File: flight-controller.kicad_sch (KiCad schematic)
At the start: 15 parts, among them J1 Conn_02x10_Odd_Even, J2 Conn_02x08_Odd_Even, J3 Conn_02x17_Odd_Even, J4 Conn_02x15_Counter_Clockwise, J5 Conn_01x02, U3 ACS773LCB-100B-PFF-T

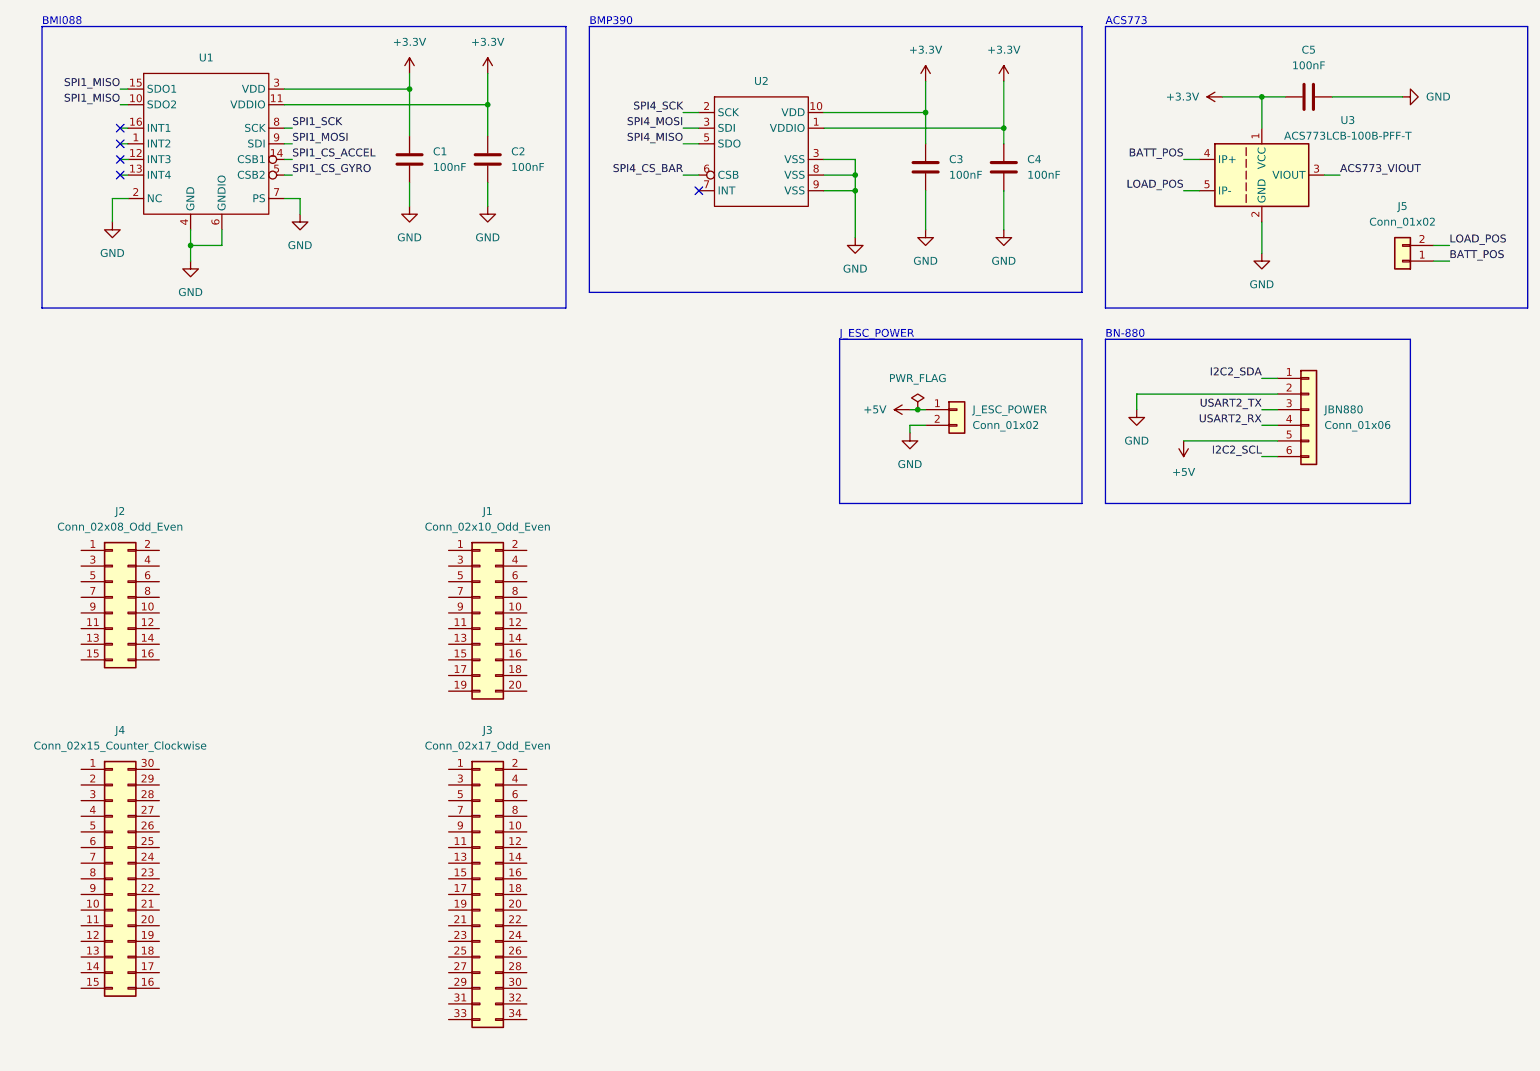
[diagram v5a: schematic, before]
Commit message: feat: Added headers of stm32 to schematic
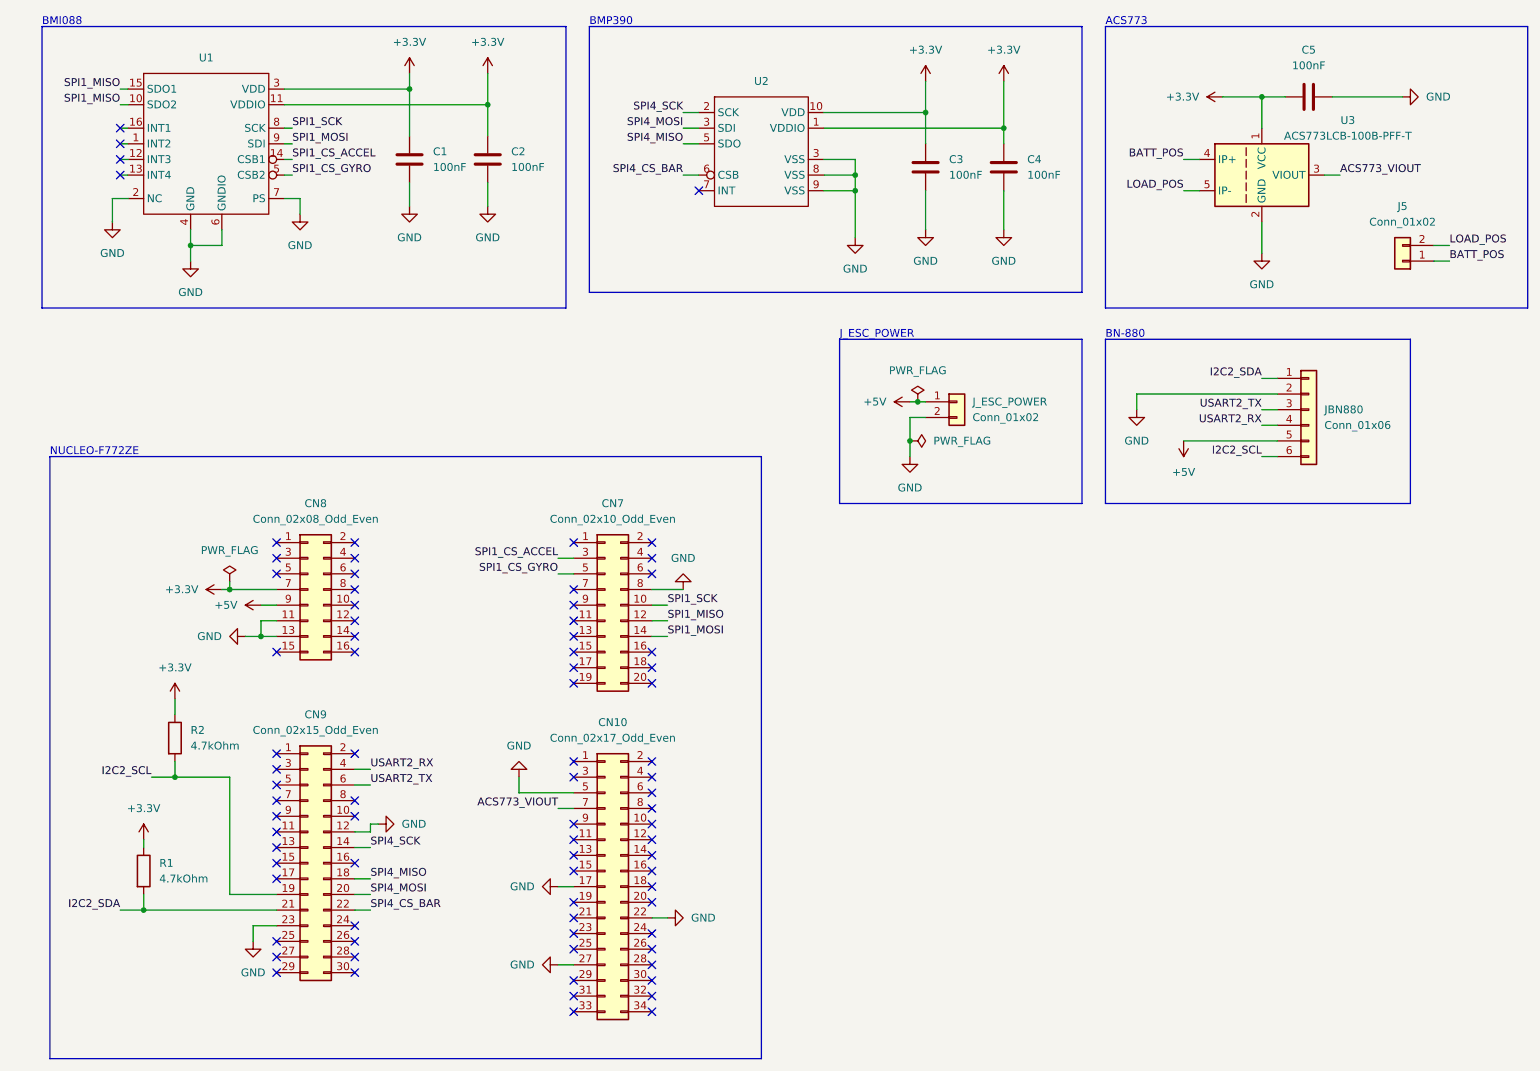
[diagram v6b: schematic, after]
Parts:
- removed J4: Conn_02x15_Counter_Clockwise, symbol Connector_Generic:Conn_02x15_Counter_Clockwise
- added CN9: Conn_02x15_Odd_Even, symbol Connector_Generic:Conn_02x15_Odd_Even
- added R1, R2: 4.7kOhm, symbol Device:R
- renumbered J3 to CN10, J1 to CN7, J2 to CN8
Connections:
- net +3.3V: now also CN8.7 (Pin_7), R1.1, R2.1
- net +5V: now also CN8.9 (Pin_9)
- net ACS773_VIOUT: now also CN10.7 (Pin_7)
- net GND: now also CN10.17 (Pin_17), CN10.22 (Pin_22), CN10.27 (Pin_27), CN10.5 (Pin_5), CN7.8 (Pin_8), CN8.11 (Pin_11), CN8.13 (Pin_13), CN9.12 (Pin_12), CN9.23 (Pin_23)
- net I2C2_SCL: now also CN9.19 (Pin_19), R2.2
- net I2C2_SDA: now also CN9.21 (Pin_21), R1.2
- net SPI1_CS_ACCEL: now also CN7.3 (Pin_3)
- net SPI1_CS_GYRO: now also CN7.5 (Pin_5)
- net SPI1_MISO: now also CN7.12 (Pin_12)
- net SPI1_MOSI: now also CN7.14 (Pin_14)
- net SPI1_SCK: now also CN7.10 (Pin_10)
- net SPI4_CS_BAR: now also CN9.22 (Pin_22)
- net SPI4_MISO: now also CN9.18 (Pin_18)
- net SPI4_MOSI: now also CN9.20 (Pin_20)
- net SPI4_SCK: now also CN9.14 (Pin_14)
- net USART2_RX: now also CN9.4 (Pin_4)
- net USART2_TX: now also CN9.6 (Pin_6)
- no-connect marks 5 -> 80
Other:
- note added: "NUCLEO-F772ZE"
- moved on the sheet: CN10, CN7, CN8, J_ESC_POWER

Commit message: feat: Added RGB LED
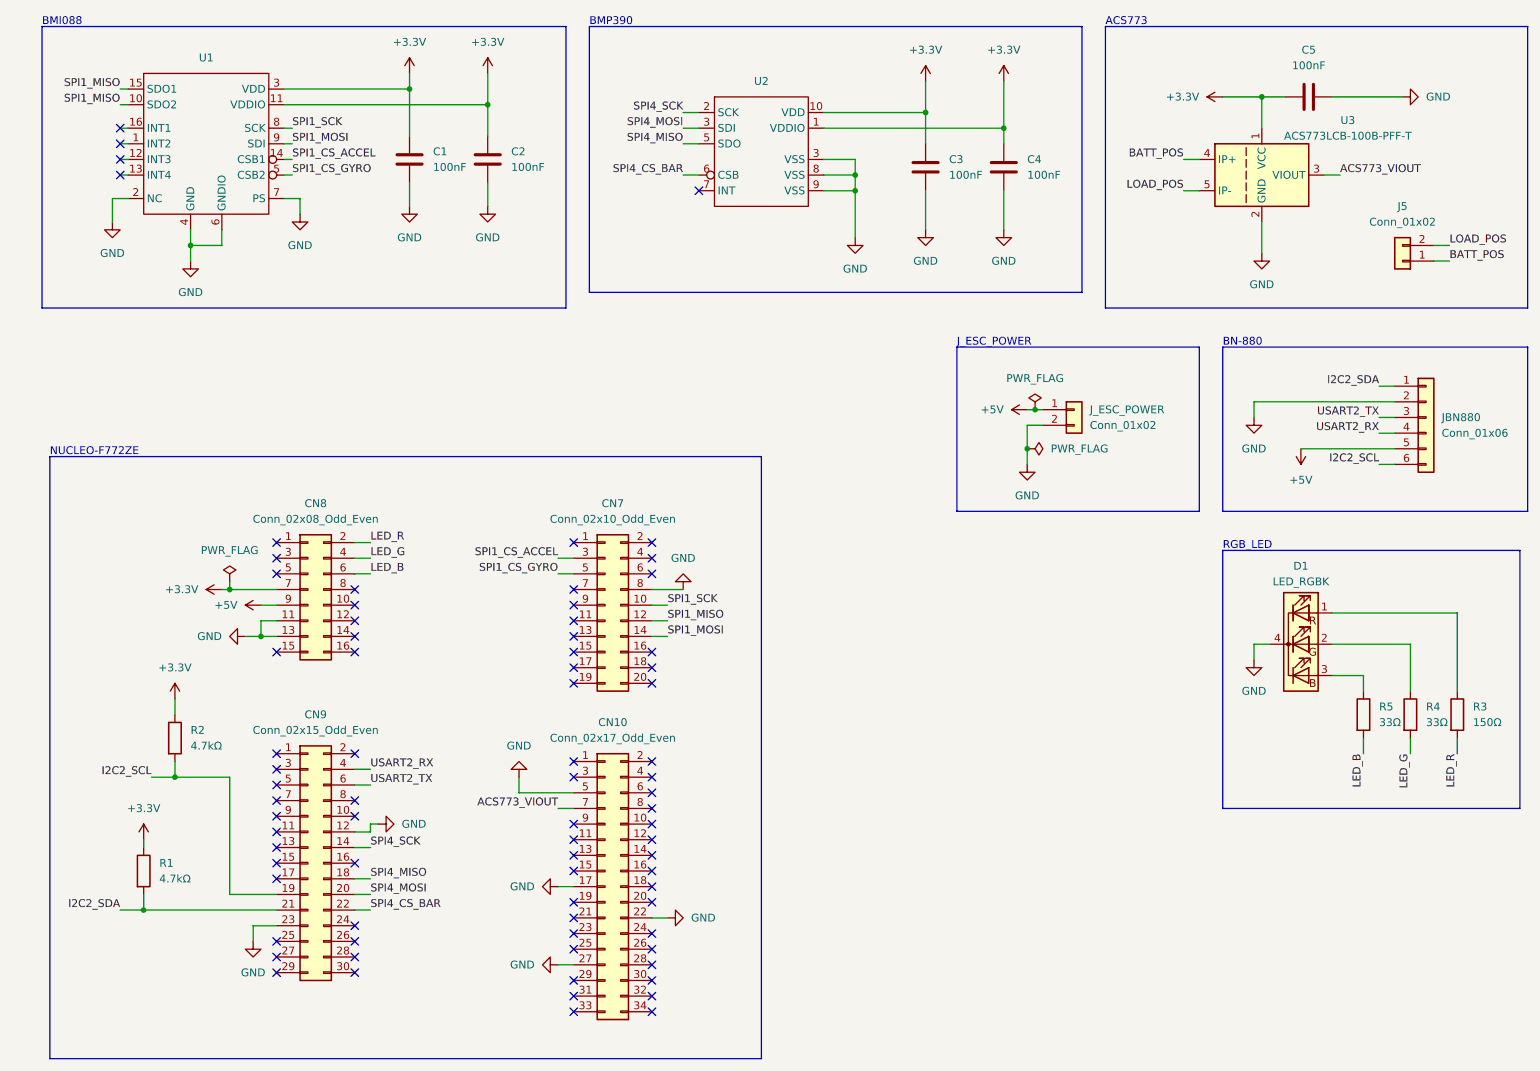
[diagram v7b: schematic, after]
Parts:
- added D1: LED_RGBK, symbol Device:LED_RGBK
- added R3: 150Ω, symbol Device:R
- added R4, R5: 33Ω, symbol Device:R
- R1, R2: value 4.7kOhm -> 4.7kΩ
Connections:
- net GND: now also D1.4 (K)
- net LED_R: now reaches CN8.2 (Pin_2)
- net LED_R: now also R3.2
- net LED_G: now reaches CN8.4 (Pin_4)
- net LED_G: now also R4.2
- net LED_B: now reaches CN8.6 (Pin_6)
- net LED_B: now also R5.2
- new net: D1.2 (GA), R4.1
- new net: D1.1 (RA), R3.1
- new net: D1.3 (BA), R5.1
- no-connect marks 80 -> 77
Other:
- note added: "RGB_LED"
- moved on the sheet: JBN880, J_ESC_POWER

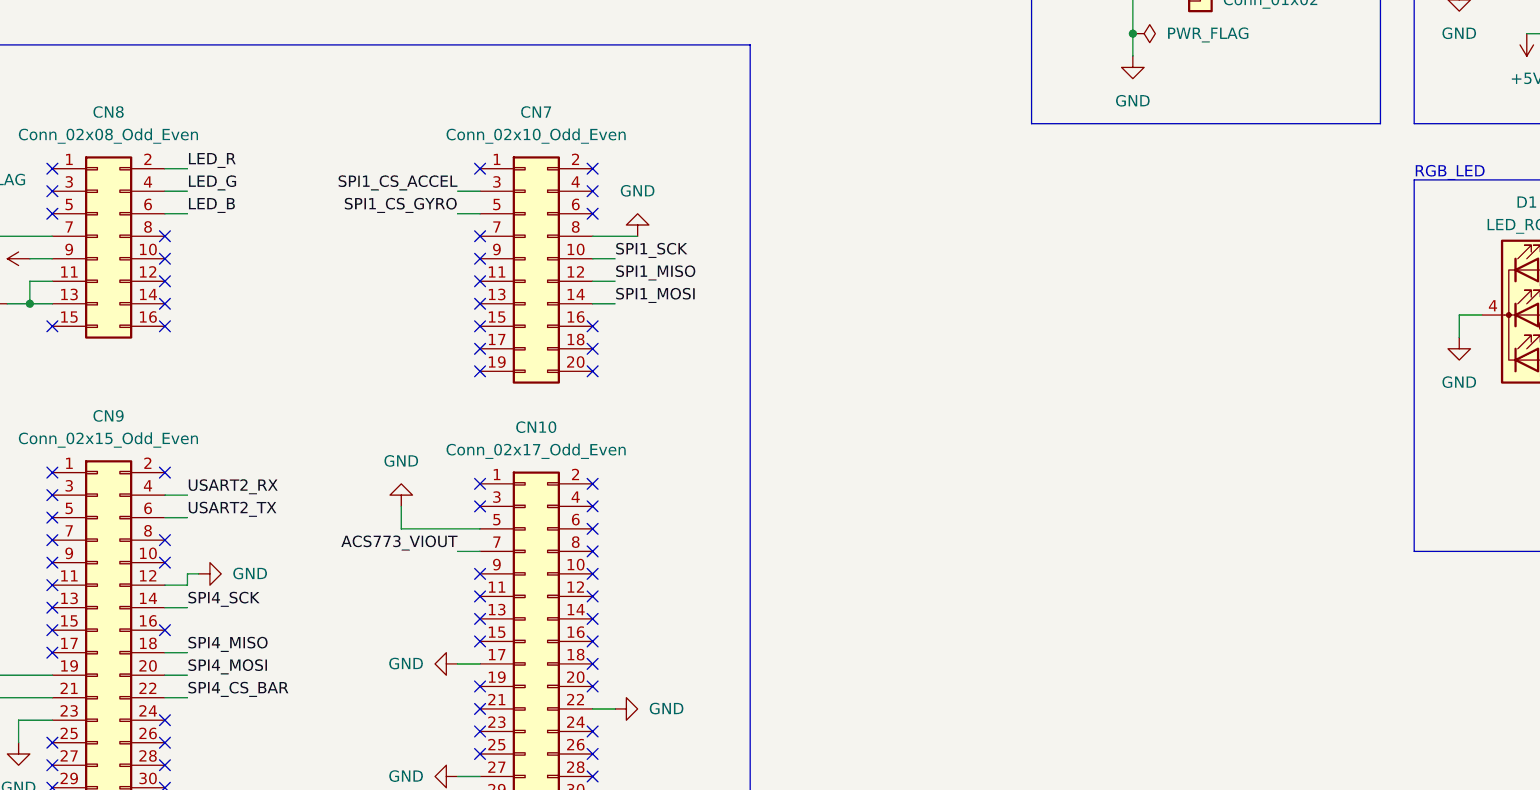
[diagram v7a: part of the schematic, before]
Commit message: feat: Added buzzer
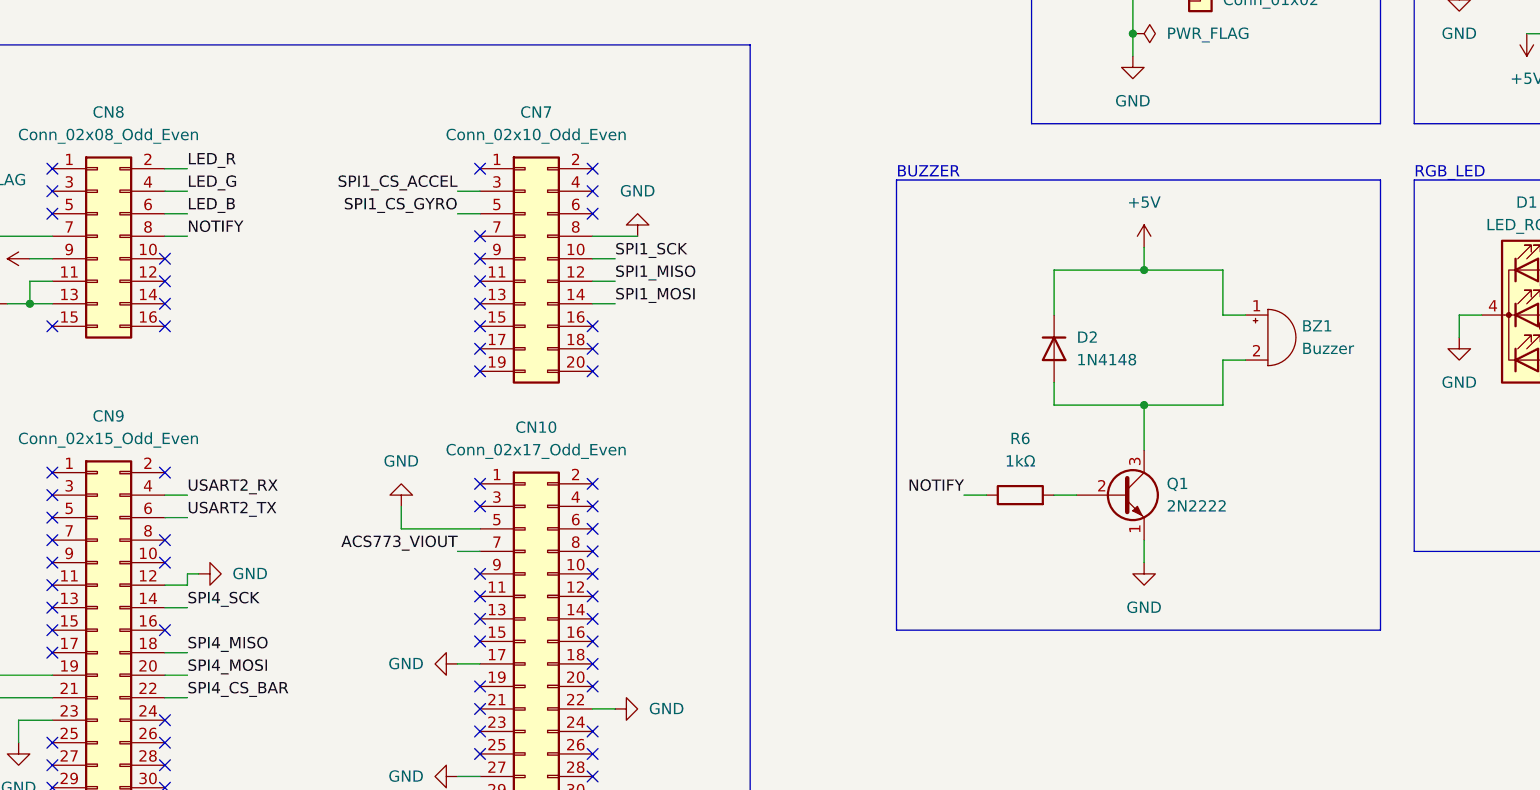
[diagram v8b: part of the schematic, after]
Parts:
- added BZ1: Buzzer, symbol Device:Buzzer
- added D2: 1N4148, Diode_THT:D_DO-35_SOD27_P7.62mm_Horizontal, symbol Diode:1N4148
- added Q1: 2N2222, Package_TO_SOT_THT:TO-39-3, symbol Transistor_BJT:2N2219
- added R6: 1kΩ, symbol Device:R
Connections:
- net +5V: now also BZ1.1 (+), D2.1 (K)
- net GND: now also Q1.1 (E)
- net NOTIFY: now reaches CN8.8 (Pin_8)
- net NOTIFY: now also R6.1
- new net: Q1.2 (B), R6.2
- new net: BZ1.2 (-), D2.2 (A), Q1.3 (C)
- no-connect marks 77 -> 76
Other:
- note added: "BUZZER"
